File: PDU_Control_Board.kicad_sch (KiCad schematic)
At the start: 235 parts, among them J1 Current_Sensor, J10 Precharge_2, J11 Shunt_2, J12 VIN_Enable, J13 1-776087-1, J15 GNDPWR, J16 VDC_OUT1_Relay, J17 VDC_OUT2_Rela, J2 Shunt_1, J20 VDC_IN, J21 VDC_OUT1, J22 VDC_OUT2, J3 SWD, J4 Precharge_1, J5 Precharge_2, J6 Shunt_2, J7 VIN_Enable, J8 Precharge_1, J9 Shunt_1, Q1 BSP75N, Q10 BC817, Q2 BSP75N, Q3 BSP75N, Q4 BSP75N, Q5 BSP75N, Q6 BC817, Q7 BC817, Q8 BC817, Q9 BC817, U1 LMV321, U2 APM32F405xG, U3 LMV321, U4 LMV321, U5 LMV321, U6 LMV321, Y2 X322516MOB4SI

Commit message: VER3.0: сделал предварительную расстановку платы
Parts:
- removed D29, D30, D31: EV200, Contactor_My:EV200, symbol Contactor_My:EV200
- removed D32, D33: SVC100A, Contactor_My:SVC100A, symbol Contactor_My:SVC100A
- removed H6: MountingHole_Pad, MountingHole:MountingHole_4.3mm_M4, symbol Mechanical:MountingHole_Pad
- removed J13: 1-776087-1, Connector_My:TE_1-776087-1, symbol Connector_My:1-776087-1
- removed J15: GNDPWR, Connector_My:Mini-Fit_01x02_Vertical, symbol Connector_Generic:Conn_01x02
- removed J16: VDC_OUT1_Relay, Connector_My:Mini-Fit_01x02_Vertical, symbol Connector_Generic:Conn_01x02
- removed J17: VDC_OUT2_Rela, Connector_My:Mini-Fit_01x02_Vertical, symbol Connector_Generic:Conn_01x02
- removed R1, R40, R41, R42, R43, R44, R45, R46, R49, R50, R51, R52, R53, R54, R55, R57: 10k, Resistor_THT:R_Axial_Power_L60.0mm_W14.0mm_P66.04mm, symbol Device:R
- added D43: BAT54S, Package_TO_SOT_SMD:SOT-23, symbol Device:D_Dual_Series_AKC_Parallel
- added J13: To_Main_Connector, Connector_Molex:Molex_Mini-Fit_Jr_5566-04A_2x02_P4.20mm_Vertical, symbol Connector_Generic:Conn_02x02_Odd_Even
- H2, H3: footprint MountingHole:MountingHole_4.3mm_M4 -> MountingHole:MountingHole_4.3mm_M4_Pad_Via
- H4: footprint MountingHole:MountingHole_4.3mm_M4_Pad_Via -> MountingHole:MountingHole_4.3mm_M4
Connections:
- net +24V: now also J13.2 (Pin_2)
- net +3.3V: now also D43.2 (K)
- net CANH: now also J13.3 (Pin_3)
- net CANL: now also J13.1 (Pin_1)
- net DC_Voltage_MCU: now also D43.3 (A)
- net GND: now also H2.1, H3.1, D43.1 (K), J13.4 (Pin_4); no longer H4.1
- net GNDPWR: now also J20.2 (Pin_2), J21.2 (Pin_2), J22.2 (Pin_2)
- net VDC_IN: no longer J20.2 (Pin_2)
- net VDC_OUT1: no longer J21.2 (Pin_2)
- net VDC_OUT2: no longer J22.2 (Pin_2)
- no-connect marks 48 -> 46
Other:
- note removed: "Блок контакторов"
- moved on the sheet: C21, C27, C28, R7, R8, R9, U4

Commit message: VER3.0: плата готова
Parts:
- added C1, C3, C74, C75: 100n, Capacitor_SMD:C_0805_2012Metric_Pad1.18x1.45mm_HandSolder, symbol Device:C_Small
- added C2, C72: 1u, Capacitor_SMD:C_0805_2012Metric_Pad1.18x1.45mm_HandSolder, symbol Device:C_Small
- added C73: 4.7u, Capacitor_SMD:C_0805_2012Metric_Pad1.18x1.45mm_HandSolder, symbol Device:C_Small
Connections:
- net +24V: now also J10.2 (Pin_2), J11.2 (Pin_2), J12.2 (Pin_2), J13.3 (Pin_3), J2.2 (Pin_2), J4.2 (Pin_2), J5.2 (Pin_2), J6.2 (Pin_2), J7.2 (Pin_2), J8.2 (Pin_2), J9.2 (Pin_2); no longer J10.1 (Pin_1), J11.1 (Pin_1), J12.1 (Pin_1), J13.2 (Pin_2), J2.1 (Pin_1), J4.1 (Pin_1), J5.1 (Pin_1), J6.1 (Pin_1), J7.1 (Pin_1), J8.1 (Pin_1), J9.1 (Pin_1)
- net +3.3V: now also C1.1, C2.1, C3.1, C72.1, C73.1, C74.1, C75.1
- net CANH: now also J13.2 (Pin_2); no longer J13.3 (Pin_3)
- net Current_SENSE: now also U2.30 (PA5); no longer U2.33 (PC4)
- net GND: now also C1.2, C2.2, C3.2, C72.2, C73.2, C74.2, C75.2
- net Precharge_1: now also U2.66 (PC9); no longer U2.68 (PA9)
- net Precharge_2: now also U2.62 (PD15); no longer U2.66 (PC9)
- net Shunt_1: now also U2.64 (PC7); no longer U2.62 (PD15)
- net Shunt_2: now also U2.60 (PD13); no longer U2.64 (PC7)
- net VDC_IN_SENSE: now also U2.33 (PC4); no longer U2.32 (PA7)
- net VDC_OUT1_SENSE: now also U2.32 (PA7); no longer U2.31 (PA6)
- net VDC_OUT2_SENSE: now also U2.31 (PA6); no longer U2.30 (PA5)
- net VIN_Enable: now also U2.68 (PA9)
- net ~{Precharge_1_ON}: now also U2.67 (PA8); no longer U2.69 (PA10)
- net ~{Precharge_2_ON}: now also U2.63 (PC6); no longer U2.67 (PA8)
- net ~{Shunt_1_ON}: now also U2.65 (PC8); no longer U2.63 (PC6)
- net ~{Shunt_2_ON}: now also U2.61 (PD14); no longer U2.65 (PC8)
- net ~{VIN_Enable_ON}: now also U2.69 (PA10); no longer U2.98 (PE1)
- net at D13.2 (A), Q5.2 (D), R12.2: now also J7.1 (Pin_1); no longer J7.2 (Pin_2)
- net at D8.2 (A), Q4.2 (D), R11.2: now also J6.1 (Pin_1); no longer J6.2 (Pin_2)
- net at D7.2 (A), Q1.2 (D), R4.2: now also J4.1 (Pin_1); no longer J4.2 (Pin_2)
- net at D20.2 (A), R73.1: now also J12.1 (Pin_1); no longer J12.2 (Pin_2)
- net at D22.2 (A), R69.1: now also J10.1 (Pin_1); no longer J10.2 (Pin_2)
- net at D4.2 (A), Q3.2 (D), R10.2: now also J5.1 (Pin_1); no longer J5.2 (Pin_2)
- net at D23.2 (A), R67.1: now also J9.1 (Pin_1); no longer J9.2 (Pin_2)
- net at D6.2 (A), Q2.2 (D), R5.2: now also J2.1 (Pin_1); no longer J2.2 (Pin_2)
- net at D24.2 (A), R65.1: now also J8.1 (Pin_1); no longer J8.2 (Pin_2)
- net at D21.2 (A), R71.1: now also J11.1 (Pin_1); no longer J11.2 (Pin_2)
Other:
- moved on the sheet: C39, C40, C41, C42, C43, D10, D11, D12, D13, D14, D20, D21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

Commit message: VER3.0: разобрался с бомом, добавил дискреты, DAC, поменял обратную свзять от контакторов, удлинил цепочку измерения высокого
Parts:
- removed Q10, Q6, Q7, Q8, Q9: BC817, Package_TO_SOT_SMD:SOT-23, symbol Transistor_BJT:BC817
- added D29, D30, D31, D32, D33: ~, Package_TO_SOT_SMD:SOT-23, symbol Device:D_Dual_Series_AKC_Parallel
- added J14: ~, Connector_PinHeader_2.54mm:PinHeader_2x04_P2.54mm_Vertical, symbol Connector_Generic:Conn_01x08
- added Q10, Q6, Q7, Q8, Q9: ~, Package_TO_SOT_SMD:SOT-23, symbol Transistor_FET:2N7002
- added R1, R40, R41, R42, R43: 10k, Resistor_SMD:R_0805_2012Metric_Pad1.20x1.40mm_HandSolder, symbol Device:R_Small
- added R44, R45, R46, R49, R50, R51: 23.7k, Resistor_SMD:R_1206_3216Metric, symbol Device:R
- added TP1, TP2: TestPoint, TestPoint:TestPoint_Loop_D1.80mm_Drill1.0mm_Beaded, symbol Connector:TestPoint
- C26, C70: Product Name (none) -> CA45-C6R3K337T
- C33, C66: Product Name (none) -> CA45L-E050K226TE400
- C39, C40, C41, C42, C43: value 2.2u -> 1u
- C62: Product Name (none) -> 293D105X9050C2TE3
- C63: Product Name (none) -> 293D106X9050E2TE3
- C64: Product Name (none) -> 293D107X96R3B2TE3
- C65: Product Name (none) -> 293D106X96R3B2TE3
- D1: value SIT65HVD232DR -> ~; Description P/N (none) -> CAN interface; Product Name (none) -> SIT65HVD232DR
- D10, D11, D12, D14, D38, D39, D9: value LED_Small -> ~; Description P/N (none) -> Blue LED; Product Name (none) -> FYLS-0805UBC
- D13, D4, D6, D7, D8: value D_Small -> ~; Description P/N (none) -> Fast recovery diode; Product Name (none) -> RS1B
- D15, D19, D20, D21, D22, D23, D24, D25, D26, D27, D40, D42: value LED_Small -> ~; Description P/N (none) -> Yellow LED; Product Name (none) -> FYLS-0805UYC
- D16: value K7803-1000R3 -> ~; Description P/N (none) -> DC/DC converter; Product Name (none) -> K7803-1000R3
- D17, D18, D28, D43, D5: value BAT54S -> ~; Description P/N (none) -> Schottky barrier diode; Product Name (none) -> BAT54S
- D2: value PESD2CAN -> ~; Description P/N (none) -> Dual Line CAN Bus Protector, 24Vrwm; Product Name (none) -> PESD2CAN
- D3: value D_Small -> ~; Description P/N (none) -> Diode; Product Name (none) -> BAS416
- D34, D35, D36: value NSI1311 -> ~; Description P/N (none) -> Isolated amplifier; Product Name (none) -> NSI1311
- D37: value WRB2403S-3WR2 -> ~; Description P/N (none) -> DC/DC converter; Product Name (none) -> WRB2403S-3WR2
- D41: value K7805-1000R3 -> ~; Description P/N (none) -> DC/DC converter; Product Name (none) -> K7805-1000R3
- J1: value Current_Sensor -> ~; Description P/N (none) -> Connector; Product Name (none) -> DS1073-01-2x2-MVT6; Purpose (none) -> Current sensor
- J10, J5: value Precharge_2 -> ~; Description P/N (none) -> Connector; Product Name (none) -> DS1073-01-2x1-MVT6; Purpose (none) -> Precharge 2
- J11, J6: value Shunt_2 -> ~; Description P/N (none) -> Connector; Product Name (none) -> DS1073-01-2x1-MVT6; Purpose (none) -> Shunt 2
- J12, J7: value VIN_Enable -> ~; Description P/N (none) -> Connector; Product Name (none) -> DS1073-01-2x1-MVT6; Purpose (none) -> VIN Enable
- J13: value To_Main_Connector -> ~; Description P/N (none) -> Connector; Product Name (none) -> DS1073-01-2x2-MVT6; Purpose (none) -> To main connector
- J2, J9: value Shunt_1 -> ~; Description P/N (none) -> Connector; Product Name (none) -> DS1073-01-2x1-MVT6; Purpose (none) -> Shunt 1
- J20: value VDC_IN -> ~; Description P/N (none) -> Connector; Product Name (none) -> DS1073-01-2x1-MVT6; Purpose (none) -> VDC IN
- J21: value VDC_OUT1 -> ~; Description P/N (none) -> Connector; Product Name (none) -> DS1073-01-2x1-MVT6; Purpose (none) -> VDC OUT1
- J22: value VDC_OUT2 -> ~; Description P/N (none) -> Connector; Product Name (none) -> DS1073-01-2x1-MVT6; Purpose (none) -> VDC OUT2
- J3: value SWD -> ~; Description P/N (none) -> Connector; Product Name (none) -> PLS-4; Purpose (none) -> SWD; Replacement (none) -> DS-1021-1x4
- J4, J8: value Precharge_1 -> ~; Description P/N (none) -> Connector; Product Name (none) -> DS1073-01-2x1-MVT6; Purpose (none) -> Precharge 1
- L1: Product Name (none) -> NLC453232T-4R7K-PF
- Q1, Q2, Q3, Q4, Q5: value BSP75N -> ~; Description P/N (none) -> Self-Protected Low Side Driver with Temperature and Current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; Product Name (none) -> BSP75N
- R15, R16, R23, R24, R88, R89: value 47k -> 23.7k
- R18, R27, R87: value 240 -> 210
- R35: value DNP -> 1k; now not fitted
- R65, R67, R69, R71, R73: value 2.2k -> 10k
- R66, R68, R70, R72, R74: value 1k -> 100
- U1, U3, U5, U6: value LMV321 -> ~; Description P/N (none) -> Low-Voltage Rail-to-Rail Output Operational Amplifiers, SOT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; Product Name (none) -> LMV321
- U2: value APM32F405xG -> ~; Description P/N (none) -> uController; Product Name (none) -> APM32F405xG
- U4: value LMV321 -> ~; footprint Package_TO_SOT_SMD:SOT-23-5_HandSoldering -> Package_TO_SOT_SMD:SOT-23-5; Description P/N (none) -> Low-Voltage Rail-to-Rail Output Operational Amplifiers, SOT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; Product Name (none) -> LMV321
- Y2: value X322516MOB4SI -> ~; Description P/N (none) -> Crystal; Product Name (none) -> X322516MOB4SI
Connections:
- net +3.3V: now also D29.2 (K), D30.2 (K), D31.2 (K), D32.2 (K), D33.2 (K)
- net Current_SENSE: now also U2.31 (PA6); no longer U2.30 (PA5)
- net DAC_OUT1: now also TP1.1
- net GND: now also D29.1 (A), D30.1 (A), D31.1 (A), D32.1 (A), D33.1 (A), Q10.2 (S), Q6.2 (S), Q7.2 (S), Q8.2 (S), Q9.2 (S), R1.1, R40.1, R41.1, R42.2, R43.1
- net VDC_IN: now also R50.2; no longer R89.2
- net VDC_IN_SENSE: now also U2.34 (PC5); no longer U2.33 (PC4)
- net VDC_OUT1: now also R46.2; no longer R15.2
- net VDC_OUT1_SENSE: now also U2.33 (PC4); no longer U2.32 (PA7)
- net VDC_OUT2: now also R45.2; no longer R23.2
- net VDC_OUT2_SENSE: now also U2.32 (PA7); no longer U2.31 (PA6)
- net ~{Precharge_1_ON}: now also D29.3 (common), Q6.3 (D)
- net ~{Precharge_2_ON}: now also D31.3 (common), Q8.3 (D)
- net ~{Shunt_1_ON}: now also D30.3 (common), Q7.3 (D)
- net ~{Shunt_2_ON}: now also D32.3 (common), Q9.3 (D)
- net ~{VIN_Enable_ON}: now also D33.3 (common), Q10.3 (D)
- net at R71.2: now also Q9.1 (G), R42.1
- net at R73.2: now also Q10.1 (G), R43.2
- net at R65.2: now also Q6.1 (G), R1.2
- net at R67.2: now also Q7.1 (G), R40.2
- net +24V_SENSE: now reaches U2.35 (PB0)
- net +24V_SENSE: now also C28.1, D43.3 (common), R8.2
- net Discete_1: now reaches U2.39 (PE8)
- net Discete_1: now also J14.1 (Pin_1)
- net Discete_2: now reaches U2.40 (PE9)
- net Discete_2: now also J14.2 (Pin_2)
- net Discete_3: now reaches U2.41 (PE10)
- net Discete_3: now also J14.3 (Pin_3)
- net Discete_4: now reaches U2.42 (PE11)
- net Discete_4: now also J14.4 (Pin_4)
- net Discete_5: now reaches U2.43 (PE12)
- net Discete_5: now also J14.5 (Pin_5)
- net Discete_6: now reaches U2.44 (PE13)
- net Discete_6: now also J14.6 (Pin_6)
- net Discete_7: now reaches U2.45 (PE14)
- net Discete_7: now also J14.7 (Pin_7)
- net Discete_8: now reaches U2.46 (PE15)
- net Discete_8: now also J14.8 (Pin_8)
- net at R69.2: now also Q8.1 (G), R41.2
- removed net DC_Voltage_MCU: C28.1, D43.3 (A), R8.2, U2.34 (PC5)
- new net: R44.2, R45.1
- new net: R50.1, R51.2
- new net: R15.2, R49.1
- new net: R46.1, R49.2
- new net: R51.1, R89.2
- new net: R23.2, R44.1
- new net DAC_OUT2: TP2.1, U2.30 (PA5)
- no-connect marks 46 -> 54
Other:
- note removed: "SWD"
- moved on the sheet: C39, C41, C42, C43, D20, D21, D23, D24, D25, D26, D27, J10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

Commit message: VER3.0: заказал плату в резоните
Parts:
- J14: now not fitted
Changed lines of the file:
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@@
 		(in_bom yes)
 		(on_board yes)
-		(dnp no)
+		(dnp yes)
 		(fields_autoplaced yes)
 		(property "Reference" "J14"

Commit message: VER1.1: обновил полигоны, закинул в резонит черновик
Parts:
- removed H4: MountingHole_Pad, MountingHole:MountingHole_4.3mm_M4, symbol Mechanical:MountingHole_Pad
- added H4: MountingHole, MountingHole:MountingHole_4.3mm_M4, symbol Mechanical:MountingHole
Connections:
- no-connect marks 54 -> 53

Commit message: VER1.1: добавил схему по госту в доки
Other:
- note added: "Разъёмы и механические отверстия"
- note added: "Схема электрическая принципиальная"
- company: (none) -> ООО "Электротранспортные технологии"
- title: (none) -> Плата управления
- moved on the sheet: C1, C10, C11, C12, C13, C14, C15, C16, C17, C18, C19, C2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

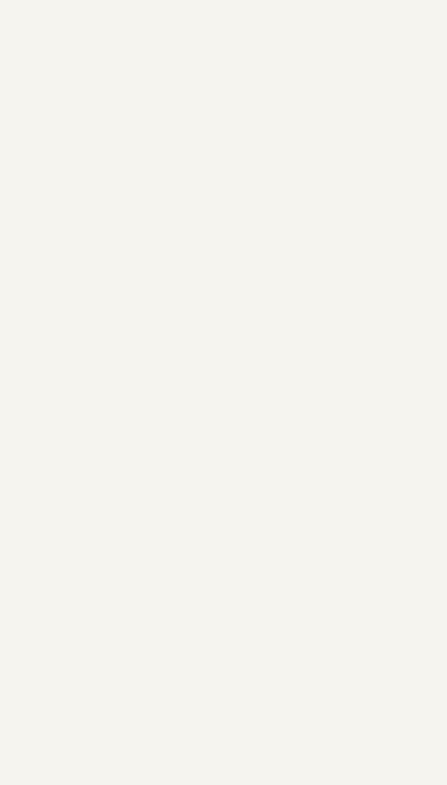
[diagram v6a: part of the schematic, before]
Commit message: VER1.1: исправил Э3
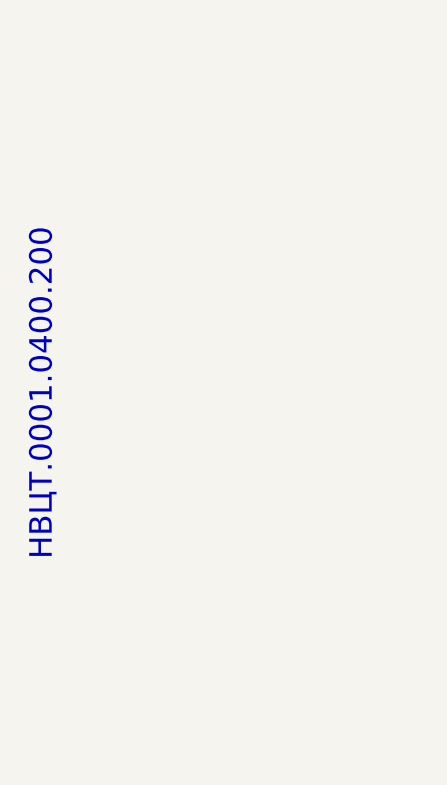
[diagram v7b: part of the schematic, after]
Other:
- note added: "НВЦТ.0001.0400.200"
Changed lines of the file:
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@@
+		)
+	)
+	(text "НВЦТ.0001.0400.200"
+		(exclude_from_sim no)
+		(at 16.51 333.248 90)
+		(effects
+			(font
+				(size 2.5 2.5)
+			)
 		)
 	)

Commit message: VER1.1: переименовал Э3
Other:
- note added: "1. Перечень элементов см. НВЦТ.0001.0400.200 ПЭ3."
- note added: "ООО "Электротранспортные"
- note added: "технологии""
- company: ООО "Электротранспортные технологии" -> (none)
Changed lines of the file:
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@@
 	(title_block
 		(title "Плата управления")
-		(company "ООО \"Электротранспортные технологии\"")
 		(comment 1 "НВЦТ.0001.0400.200 Э3")
 		(comment 2 "Филатов А.С.")
@@
 		)
 	)
+	(text "1. Перечень элементов см. НВЦТ.0001.0400.200 ПЭ3."
+		(exclude_from_sim no)
+		(at 704.342 512.826 0)
+		(effects
+			(font
+				(size 3.5 3.5)
+			)
+		)
+	)
 	(text "Питание 5В"
 		(exclude_from_sim no)
@@
 		)
 	)
+	(text "ООО \"Электротранспортные"
+		(exclude_from_sim no)
+		(at 811.022 578.866 0)
+		(effects
+			(font
+				(size 2.5 2.5)
+			)
+		)
+	)
+	(text "технологии\""
+		(exclude_from_sim no)
+		(at 811.022 583.184 0)
+		(effects
+			(font
+				(size 2.5 2.5)
+			)
+		)
+	)
